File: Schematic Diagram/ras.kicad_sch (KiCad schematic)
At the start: 22 parts, among them Q1 S8050, SW1 SW_Push, SW2 SW_Push, SW3 SW_Push, SW4 SW_Push, SW5 RotaryEncoder_Switch, SW6 SW_Push

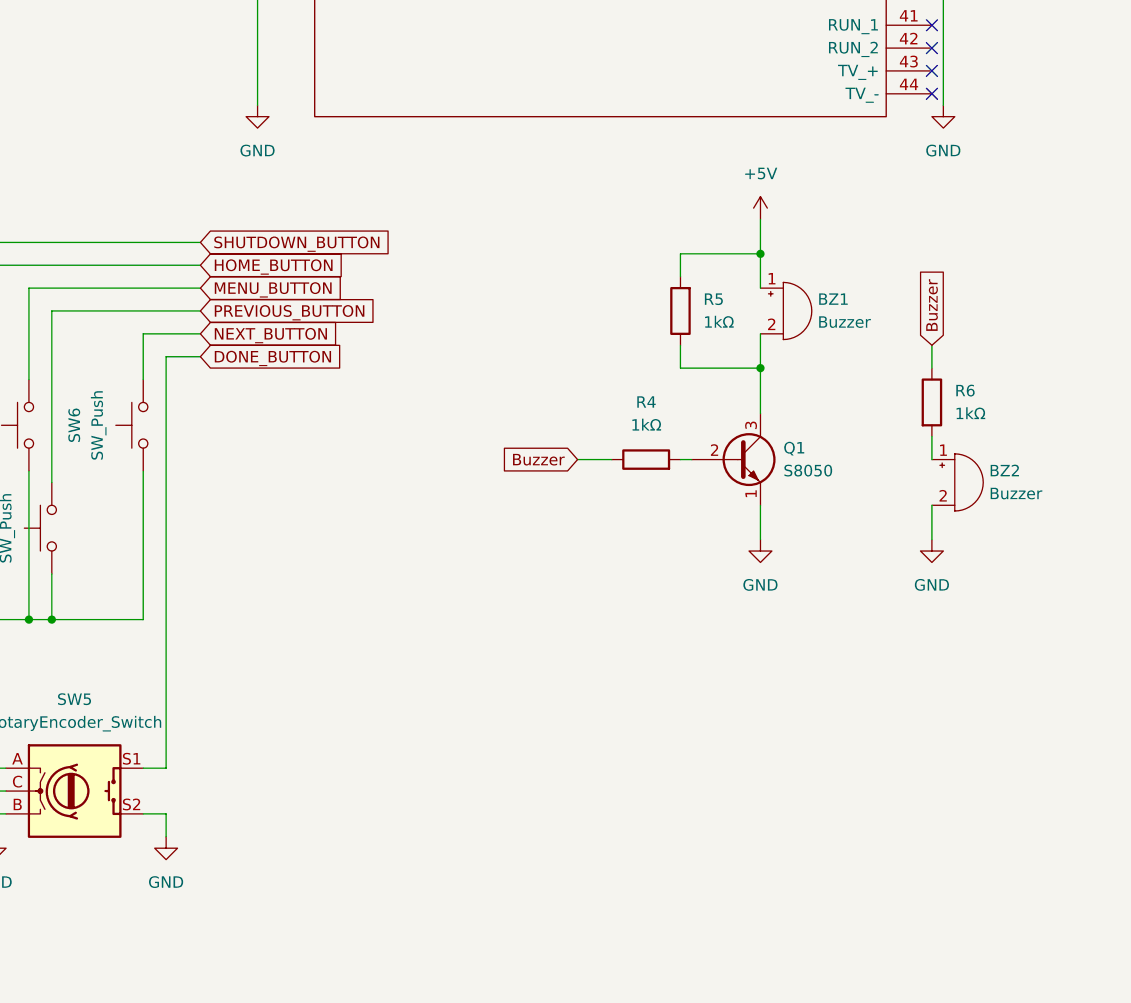
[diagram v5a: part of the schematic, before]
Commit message: create fp-lib and fp-table
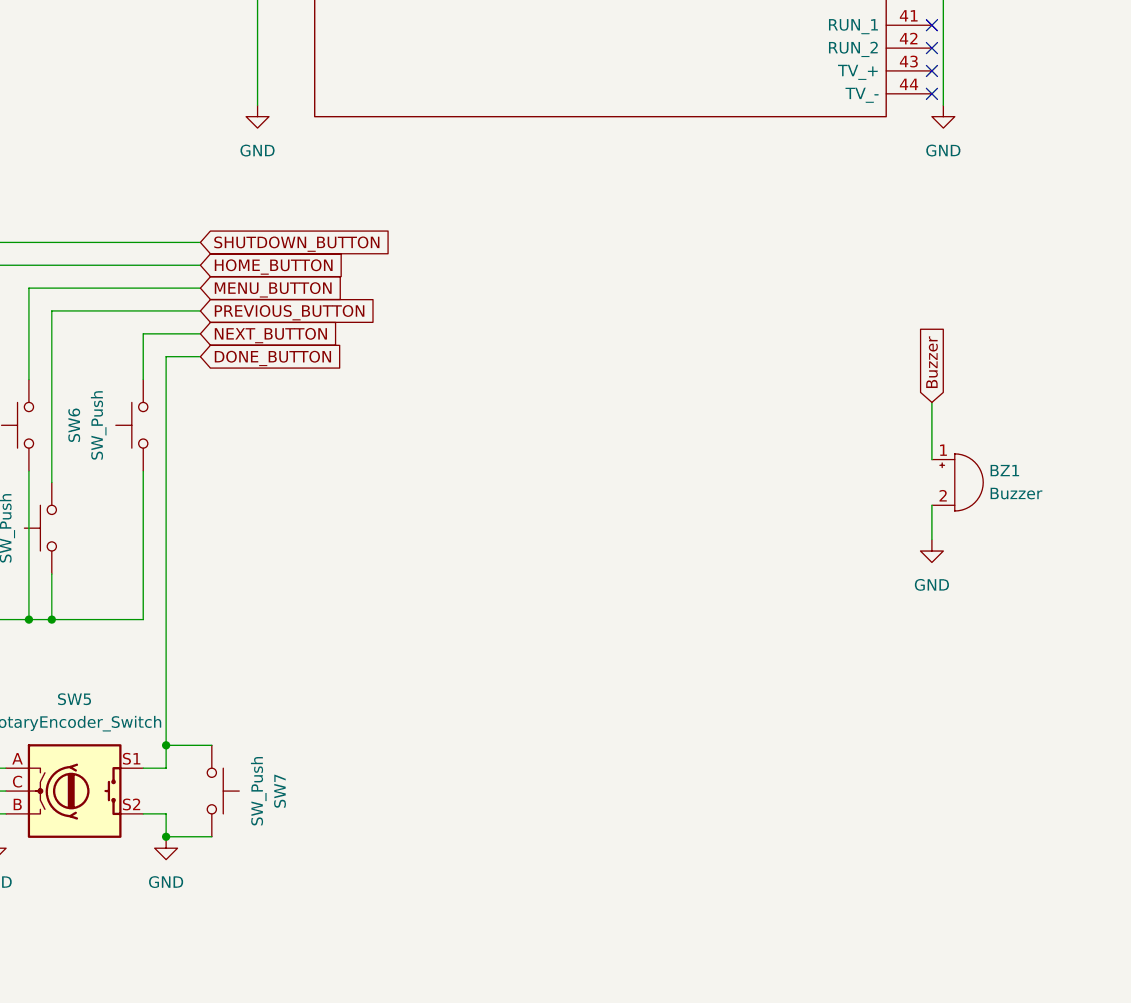
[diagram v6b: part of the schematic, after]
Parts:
- removed BZ1: Buzzer, symbol Device:Buzzer
- removed Q1: S8050, Package_TO_SOT_THT:TO-92_Inline, symbol Transistor_BJT:S8050
- removed R4, R5, R6: 1kΩ, symbol Device:R
- added SW7: SW_Push, project:SW_PUSH_6mm, symbol Switch:SW_Push
- BZ1: renamed from BZ2; footprint (none) -> project:Buzzer_12x9.5RM7.6
- D1, D2, D3: footprint (none) -> project:LED_D5.0mm
- LCD_Module1: footprint (none) -> project:WC1602A
- R1, R2, R3: footprint (none) -> project:R_Axial_DIN0207_L6.3mm_D2.5mm_P7.62mm_Horizontal
- RFID1: footprint (none) -> project:RFID-RC522
- RP1: footprint RASPBERRYPI -> project:PinSocket_2x20_P2.54mm_Vertical
- SW1, SW2, SW3, SW4, SW6: footprint (none) -> project:SW_PUSH_6mm
- SW5: footprint (none) -> project:RotaryEncoder_Alps_EC12E-Switch_Vertical_H20mm
- U1: footprint (none) -> project:DS3231M
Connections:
- net Buzzer: now also BZ1.1 (-)
- net DONE_BUTTON: now also SW7.1
- net GND: now also SW7.2

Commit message: fix fp
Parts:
- RP1: footprint project:PinSocket_2x20_P2.54mm_Vertical -> project:raspberrypi3
- SW1: value SW_Push -> SHUTDOWN
- SW2: value SW_Push -> HOME
- SW3: value SW_Push -> MENU
- SW4: value SW_Push -> PREVIOUS
- SW6: value SW_Push -> NEXT
- SW7: value SW_Push -> DONE
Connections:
- no-connect marks 16 -> 12
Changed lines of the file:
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@@
 	)
 	(no_connect
-		(at 213.36 82.55)
-	)
-	(no_connect
-		(at 213.36 74.93)
-	)
-	(no_connect
 		(at 139.7 41.91)
 	)
@@
 	)
 	(no_connect
-		(at 213.36 80.01)
-	)
-	(no_connect
 		(at 213.36 64.77)
 	)
@@
 	)
 	(no_connect
-		(at 213.36 77.47)
-	)
-	(no_connect
 		(at 139.7 54.61)
 	)
@@
 			)
 		)
-		(property "Value" "SW_Push"
+		(property "Value" "DONE"
 			(at 138.43 160.02 0)
 			(effects
@@
 			)
 		)
-		(property "Footprint" "project:PinSocket_2x20_P2.54mm_Vertical"
+		(property "Footprint" "project:raspberrypi3"
 			(at 170.18 -1.27 0)
 			(effects
@@
 		(pin "40"
 		)
-		(pin "41"
-		)
-		(pin "42"
-		)
-		(pin "43"
-		)
-		(pin "44"
-		)
 		(pin "5"
 		)
@@
 			)
 		)
-		(property "Value" "SW_Push"
+		(property "Value" "PREVIOUS"
 			(at 110.49 130.81 0)
 			(effects
@@
 			)
 		)
-		(property "Value" "SW_Push"
+		(property "Value" "HOME"
 			(at 97.79 130.81 0)
 			(effects
@@
 			)
 		)
-		(property "Value" "SW_Push"
+		(property "Value" "SHUTDOWN"
 			(at 95.25 119.38 0)
 			(effects
@@
 			)
 		)
-		(property "Value" "SW_Push"
+		(property "Value" "MENU"
 			(at 107.95 119.38 0)
 			(effects
@@
 			)
 		)
-		(property "Value" "SW_Push"
+		(property "Value" "NEXT"
 			(at 120.65 119.38 0)
 			(effects

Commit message: pass DRC checks
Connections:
- net GND: no longer RP1.34 (GND_7)
- no-connect marks 12 -> 13
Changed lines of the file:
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@@
 	(paper "A4")
 	(junction
-		(at 214.63 62.23)
-		(diameter 0)
-		(color 0 0 0 0)
-	)
-	(junction
 		(at 39.37 120.65)
 		(diameter 0)
@@
 	)
 	(no_connect
+		(at 213.36 62.23)
+	)
+	(no_connect
 		(at 139.7 54.61)
 	)
@@
 	(wire
 		(pts
-			(xy 214.63 62.23) (xy 214.63 83.82)
-		)
-		(stroke
-			(width 0)
-			(type default)
-		)
-	)
-	(wire
-		(pts
 			(xy 132.08 111.76) (xy 128.27 111.76)
 		)
@@
 	(wire
 		(pts
-			(xy 213.36 62.23) (xy 214.63 62.23)
-		)
-		(stroke
-			(width 0)
-			(type default)
-		)
-	)
-	(wire
-		(pts
 			(xy 107.95 157.48) (xy 110.49 157.48)
 		)
@@
 	(wire
 		(pts
-			(xy 214.63 57.15) (xy 214.63 62.23)
-		)
-		(stroke
+			(xy 214.63 57.15) (xy 214.63 83.82)
+		)
+		(stroke
